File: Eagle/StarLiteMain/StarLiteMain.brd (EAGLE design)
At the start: 68.6 x 83.8 mm, 36 parts, among them U1 UPDUINO3P0, U2 74AHCT245N

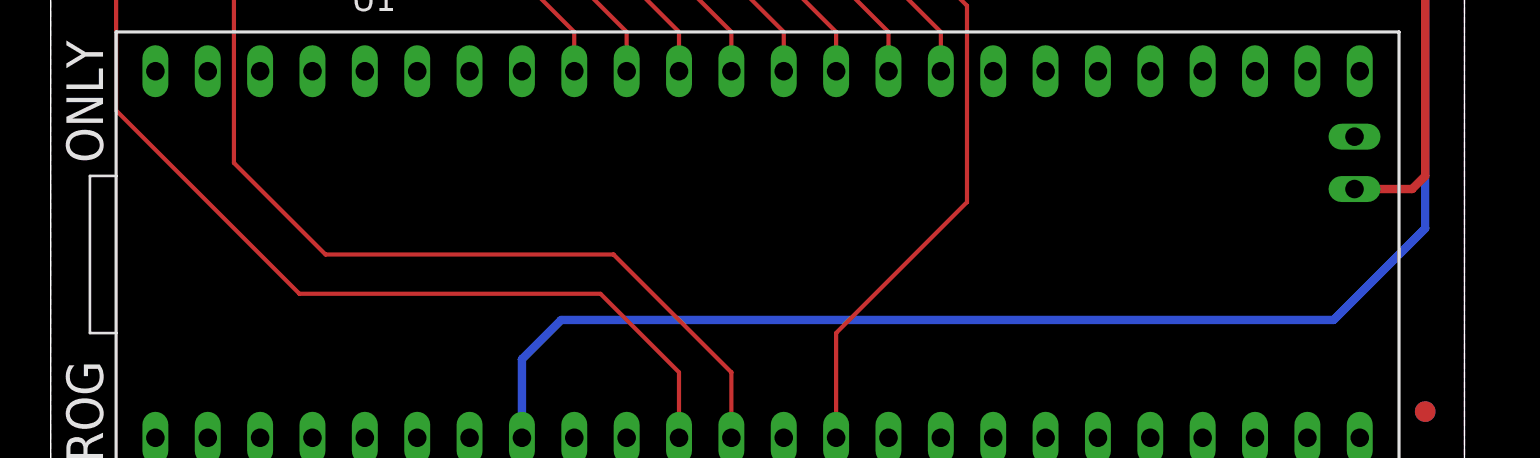
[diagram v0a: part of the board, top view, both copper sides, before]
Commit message: Moved 5V & GND Holes
Moved 5V & GND hole pair
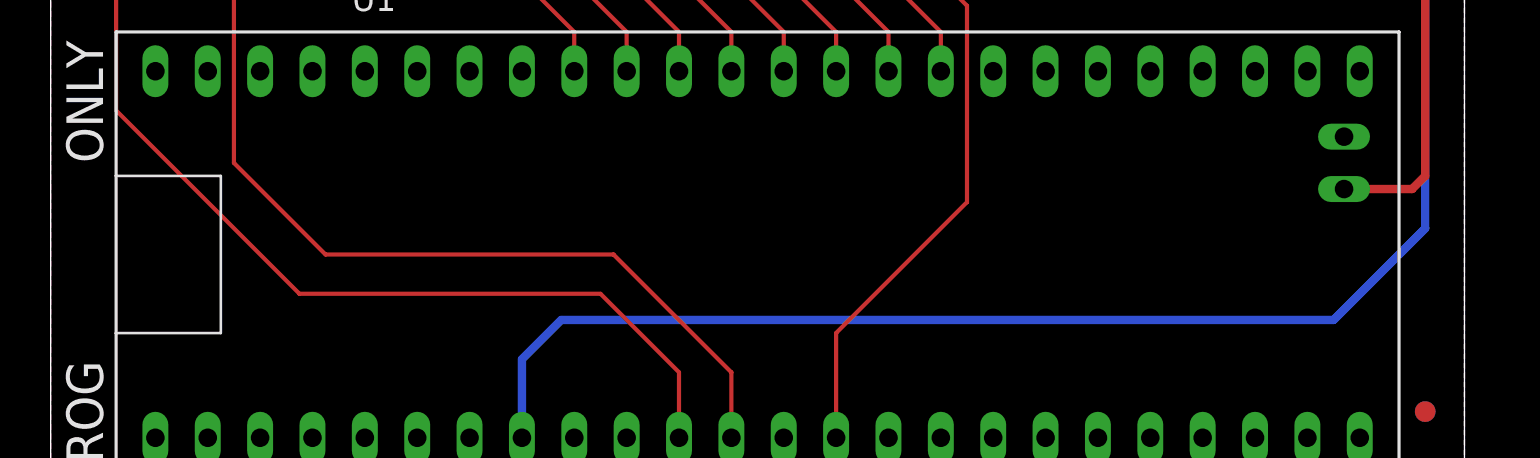
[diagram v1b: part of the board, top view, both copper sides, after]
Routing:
- net PWR2F: track 77.9 -> 78.4 mm
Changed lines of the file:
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@@
 <wire x1="65.405" y1="26.67" x2="66.675" y2="25.4" width="0.4064" layer="1"/>
 <wire x1="66.675" y1="16.51" x2="66.04" y2="15.875" width="0.4064" layer="1"/>
-<wire x1="66.04" y1="15.875" x2="63.246" y2="15.875" width="0.4064" layer="1"/>
+<wire x1="66.04" y1="15.875" x2="62.738" y2="15.875" width="0.4064" layer="1"/>
 <wire x1="66.675" y1="25.4" x2="66.675" y2="16.51" width="0.4064" layer="1"/>
 <wire x1="65.405" y1="26.67" x2="66.675" y2="25.4" width="0.4064" layer="16"/>
